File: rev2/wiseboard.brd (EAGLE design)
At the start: 50 x 50 mm, 57 parts, among them IC1 LT1945, IC2 LM358, IC3 L79L15, IC4 L78L15, IC5 W25Q, IC8 IC6, IC9 BQ24210DQCT, J1 BAT_CON, J2 SOL_CON, J3 PROG_HEADER, Q1 IRLM, SW1 SPST_TACT-KMR2, SW2 SPST_TACT-KMR2, U3 ESP-WROOM-03

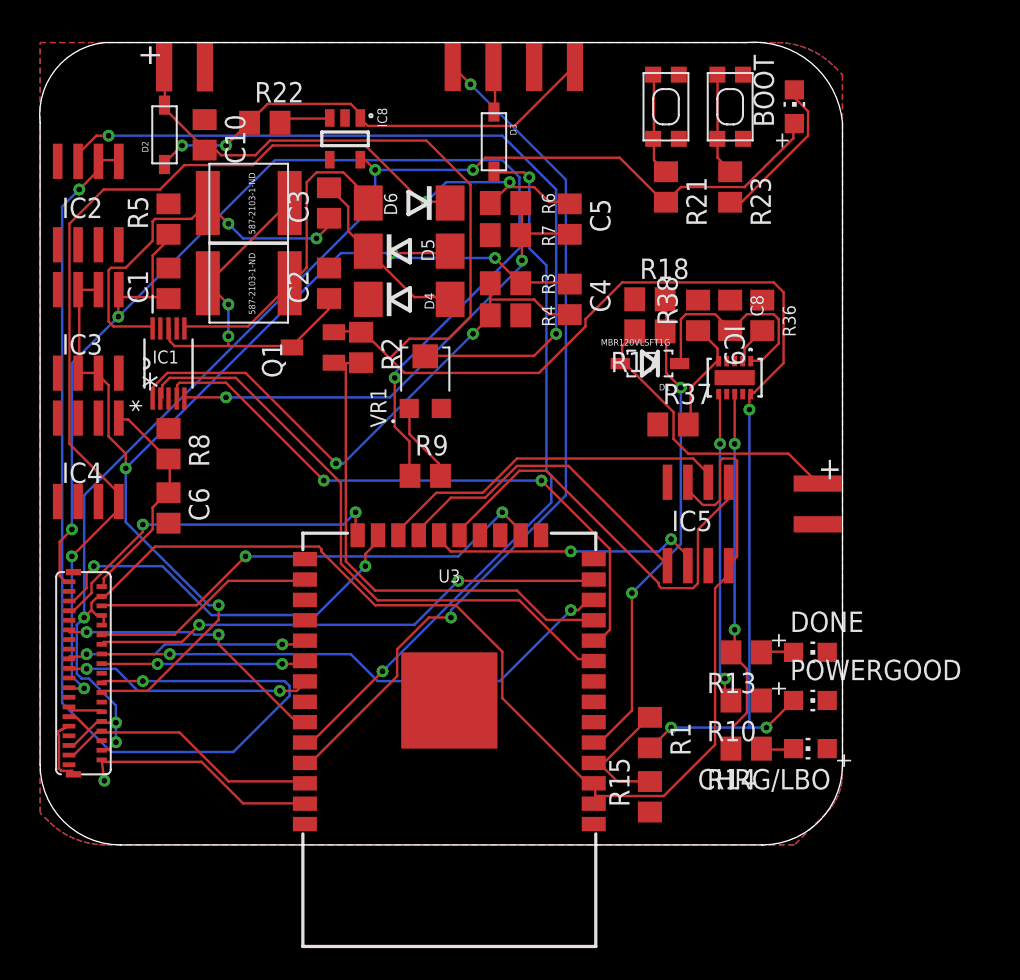
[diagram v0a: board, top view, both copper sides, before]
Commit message: Add button header, 2nd revision of pcb layout, mess up a bunch of save files
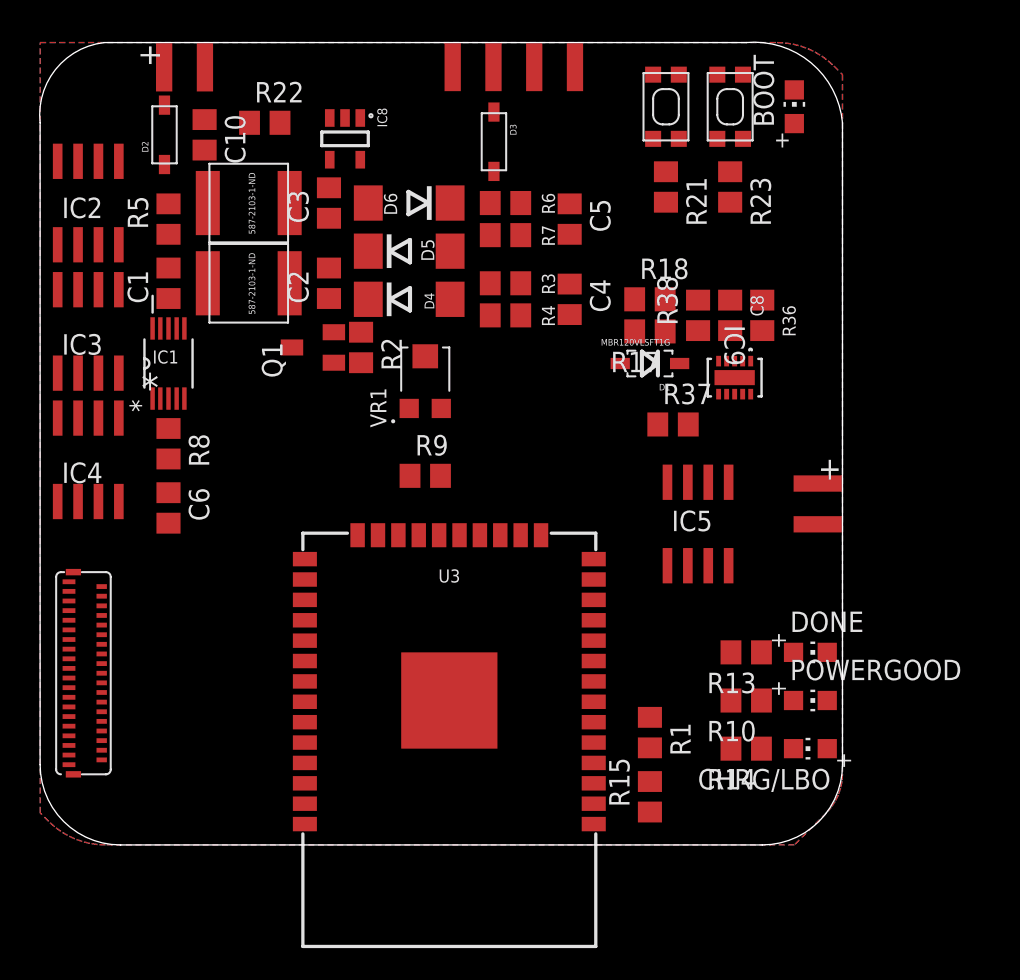
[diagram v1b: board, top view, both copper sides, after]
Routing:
- net +3V3: track 160.8 -> 0.00 mm, vias 5 -> 0
- net VBAT: track 109.2 -> 0.00 mm, vias 3 -> 0
- net -15V: track 79.7 -> 0.00 mm, vias 3 -> 0
- net -20V: track 73.4 -> 0.00 mm, vias 4 -> 0
- net +22V: track 71.7 -> 0.00 mm, vias 4 -> 0
- net VCOMMON: track 65.5 -> 0.00 mm, vias 2 -> 0
- net TXD: track 54.0 -> 0.00 mm, vias 2 -> 0
- net N$1: track 49.8 -> 0.00 mm, vias 2 -> 0
- net RXD: track 44.7 -> 0.00 mm, vias 2 -> 0
- net POSEN: track 38.5 -> 0.00 mm, vias 2 -> 0
- net NEGEN: track 38.3 -> 0.00 mm
- net NFB1: track 35.6 -> 0.00 mm, vias 2 -> 0
- net D4: track 33.4 -> 0.00 mm, vias 2 -> 0
- net D2: track 32.4 -> 0.00 mm, vias 2 -> 0
- net FB2: track 31.5 -> 0.00 mm, vias 2 -> 0
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
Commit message: fix file troubles, semi finalize layout, fix component labels
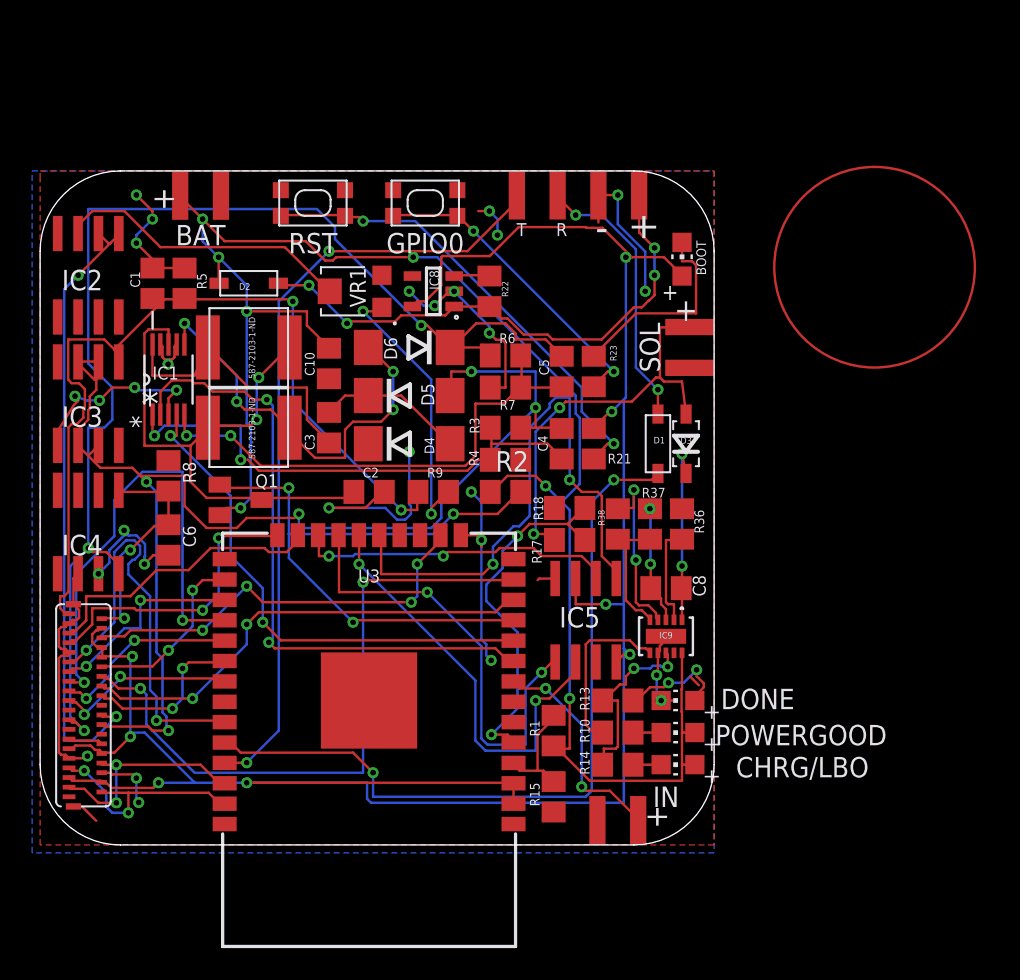
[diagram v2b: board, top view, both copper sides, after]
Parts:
- added J4: BUT_CON, WISE:EDGE_CON_2
- moved SW2 22.8 mm to (17.0, 40.0), turned to 0 degrees
- moved D3 21.4 mm to (38.5, 25.0)
- moved SW1 19.9 mm to (24.0, 40.0), turned to 0 degrees
- moved R22 17.5 mm to (28.0, 34.5), turned to 90 degrees
- moved C8 17.5 mm to (39.0, 16.0), turned to 0 degrees
- moved IC9 16.7 mm to (39.0, 13.0)
- moved R21 16.6 mm to (34.5, 25.0), turned to 90 degrees
- moved C10 16.2 mm to (18.0, 30.0), turned to 90 degrees
- moved R23 14.3 mm to (34.5, 29.5), turned to 90 degrees
- moved C3 14.0 mm to (18.0, 26.0)
- moved R17 13.9 mm to (33.0, 19.0)
- moved R18 13.9 mm to (33.0, 21.0)
- moved R36 13.9 mm to (40.0, 20.0)
- moved R38 13.9 mm to (36.0, 20.0)
- moved C2 13.2 mm to (20.5, 22.0), turned to 0 degrees
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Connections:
- net VCC renamed +5V
- removed net N$46: U3.8
- new net BUT_CON: J4.1, U3.8
- net GND: now also J4.2
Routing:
- net +3V3: track 0.00 -> 137.9 mm, vias 0 -> 8
- net GND: track 0.00 -> 116.2 mm, vias 0 -> 31
- net VBAT: track 0.00 -> 107.3 mm, vias 0 -> 7
- net -20V: track 0.00 -> 79.0 mm, vias 0 -> 5
- net +22V: track 0.00 -> 77.2 mm, vias 0 -> 3
- net -15V: track 0.00 -> 55.3 mm, vias 0 -> 2
- net TXD: track 0.00 -> 48.8 mm, vias 0 -> 2
- net RXD: track 0.00 -> 48.2 mm, vias 0 -> 2
- net D2: track 0.00 -> 41.2 mm, vias 0 -> 2
- net SUP_CTRL: track 0.00 -> 40.0 mm, vias 0 -> 3
- net NEGEN: track 0.00 -> 40.0 mm, vias 0 -> 2
- net VCOMMON: track 0.00 -> 38.8 mm, vias 0 -> 2
- net IC5: track 0.00 -> 35.9 mm, vias 0 -> 2
- net N$4: track 0.00 -> 35.7 mm, vias 0 -> 2
- net +5V: track 0.00 -> 33.7 mm, vias 0 -> 4
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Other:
- board size 50 x 50 mm -> 42 x 42 mm
- board text added: "+"
- board text added: "-"
- board text added: "BAT"
- board text added: "GPIO0"
- board text added: "IN"
- board text added: "R"
- board text added: "RST"
- board text added: "SOL"
- board text added: "T"
